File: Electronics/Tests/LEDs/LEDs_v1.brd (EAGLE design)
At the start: 17.4 x 17.8 mm, 3 parts

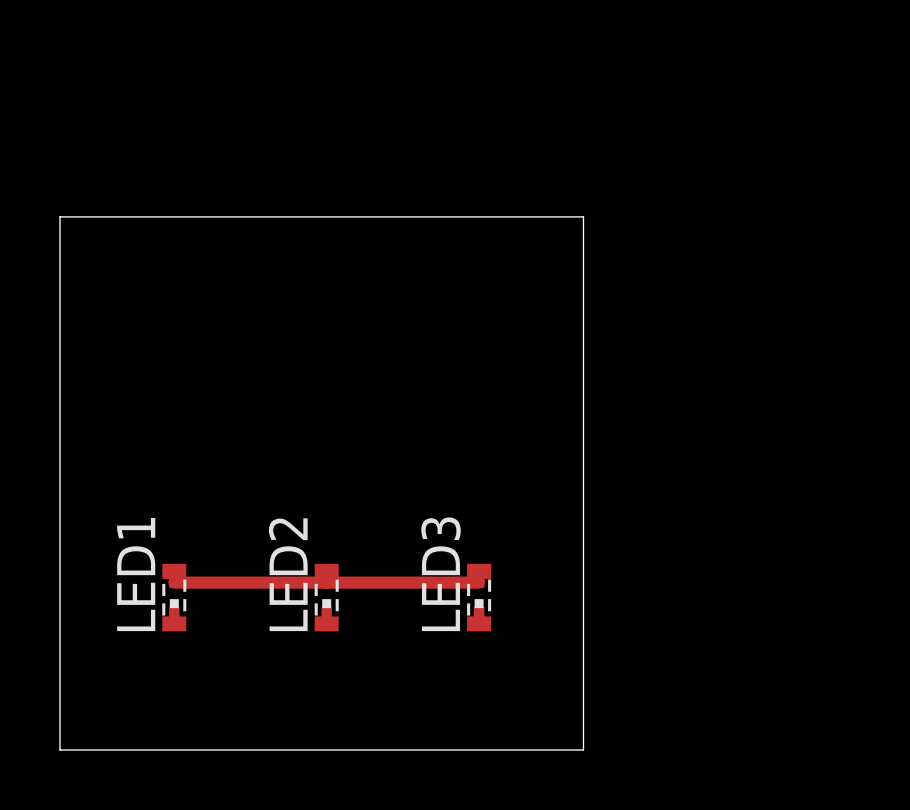
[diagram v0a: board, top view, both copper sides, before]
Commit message: Rear brake lamp started
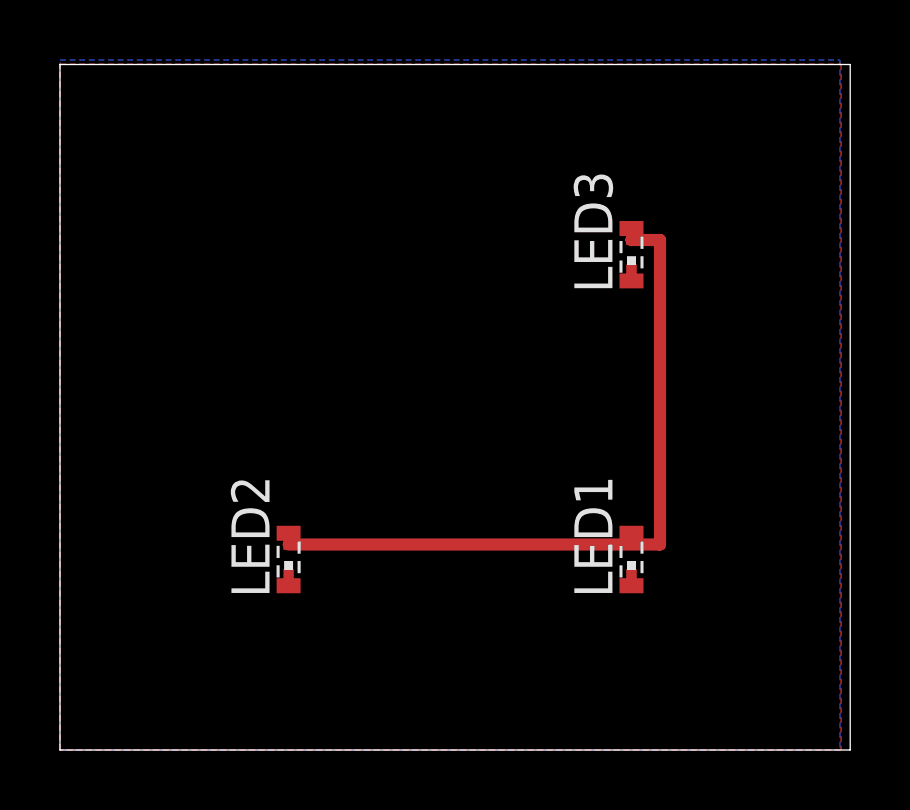
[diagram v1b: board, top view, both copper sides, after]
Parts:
- moved LED1 15.3 mm to (19.1, 6.35)
- moved LED3 12.5 mm to (19.1, 16.5)
- moved LED2 1.80 mm to (7.62, 6.35)
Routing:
- net GND: track 10.2 -> 23.5 mm
- added copper zone on layer 1, net GND
- added copper zone on layer 16, net GND
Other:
- board size 17.4 x 17.8 mm -> 26.3 x 22.9 mm
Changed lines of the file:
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@@
 <setting verticaltext="up"/>
 </settings>
-<grid distance="0.05" unitdist="inch" unit="inch" style="lines" multiple="1" display="no" altdistance="0.025" altunitdist="inch" altunit="inch"/>
+<grid distance="1" unitdist="mm" unit="mm" style="lines" multiple="1" display="yes" altdistance="0.5" altunitdist="mm" altunit="mm"/>
 <layers>
 <layer number="1" name="Top" color="4" fill="1" visible="yes" active="yes"/>
@@
 <board>
 <plain>
-<wire x1="0" y1="0" x2="17.45" y2="0" width="0" layer="20"/>
-<wire x1="17.45" y1="0" x2="17.45" y2="17.77" width="0" layer="20"/>
-<wire x1="17.45" y1="17.77" x2="0" y2="17.77" width="0" layer="20"/>
-<wire x1="0" y1="17.77" x2="0" y2="0" width="0" layer="20"/>
-<dimension x1="0" y1="17.77" x2="0" y2="0" x3="-3.81" y3="8.885" textsize="1.778" layer="20"/>
-<dimension x1="0" y1="0" x2="17.45" y2="0" x3="8.725" y3="-3.81" textsize="1.778" layer="20"/>
+<wire x1="0" y1="0" x2="26.34" y2="0" width="0" layer="20"/>
+<wire x1="26.34" y1="0" x2="26.34" y2="22.85" width="0" layer="20"/>
+<wire x1="26.34" y1="22.85" x2="0" y2="22.85" width="0" layer="20"/>
+<wire x1="0" y1="22.85" x2="0" y2="0" width="0" layer="20"/>
 </plain>
 <attributes>
@@
 </autorouter>
 <elements>
-<element name="LED1" library="led" package="SMARTLED-TTW" value="" x="3.81" y="5.08"/>
-<element name="LED2" library="led" package="SMARTLED-TTW" value="" x="8.89" y="5.08"/>
-<element name="LED3" library="led" package="SMARTLED-TTW" value="" x="13.97" y="5.08"/>
+<element name="LED1" library="led" package="SMARTLED-TTW" value="" x="19.05" y="6.35"/>
+<element name="LED2" library="led" package="SMARTLED-TTW" value="" x="7.62" y="6.35"/>
+<element name="LED3" library="led" package="SMARTLED-TTW" value="" x="19.05" y="16.51"/>
 </elements>
 <signals>
@@
 <contactref element="LED2" pad="C@1"/>
 <contactref element="LED3" pad="C@1"/>
-<wire x1="3.81" y1="5.58" x2="8.89" y2="5.58" width="0.4064" layer="1"/>
-<wire x1="8.89" y1="5.58" x2="13.97" y2="5.58" width="0.4064" layer="1"/>
+<polygon width="0.4064" layer="1">
+<vertex x="0" y="22.86"/>
+<vertex x="26.035" y="22.86"/>
+<vertex x="26.035" y="0"/>
+<vertex x="0" y="0"/>
+</polygon>
+<polygon width="0.4064" layer="16">
+<vertex x="0" y="23"/>
+<vertex x="26" y="23"/>
+<vertex x="26" y="0"/>
+<vertex x="0" y="0"/>
+</polygon>
+<wire x1="7.62" y1="6.85" x2="20" y2="6.85" width="0.4064" layer="1"/>
+<wire x1="20" y1="6.85" x2="20" y2="17" width="0.4064" layer="1"/>
+<wire x1="20" y1="17" x2="19.05" y2="17" width="0.4064" layer="1"/>
+<wire x1="19.05" y1="17" x2="19.05" y2="17.01" width="0.4064" layer="1"/>
+<wire x1="20" y1="6.85" x2="19.05" y2="6.85" width="0" layer="19" extent="1-1"/>
 </signal>
 <signal name="N$1">
